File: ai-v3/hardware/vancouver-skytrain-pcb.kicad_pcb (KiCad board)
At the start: 2 copper layers, 150 x 86.2 mm, 85 parts, among them SW1 TS-1187A-B-A-B, SW2 TS-1187A-B-A-B, SW3 TS-1187A-B-A-B, SW4 TS-1187A-B-A-B, U1 XIAO-RP2040-DIP

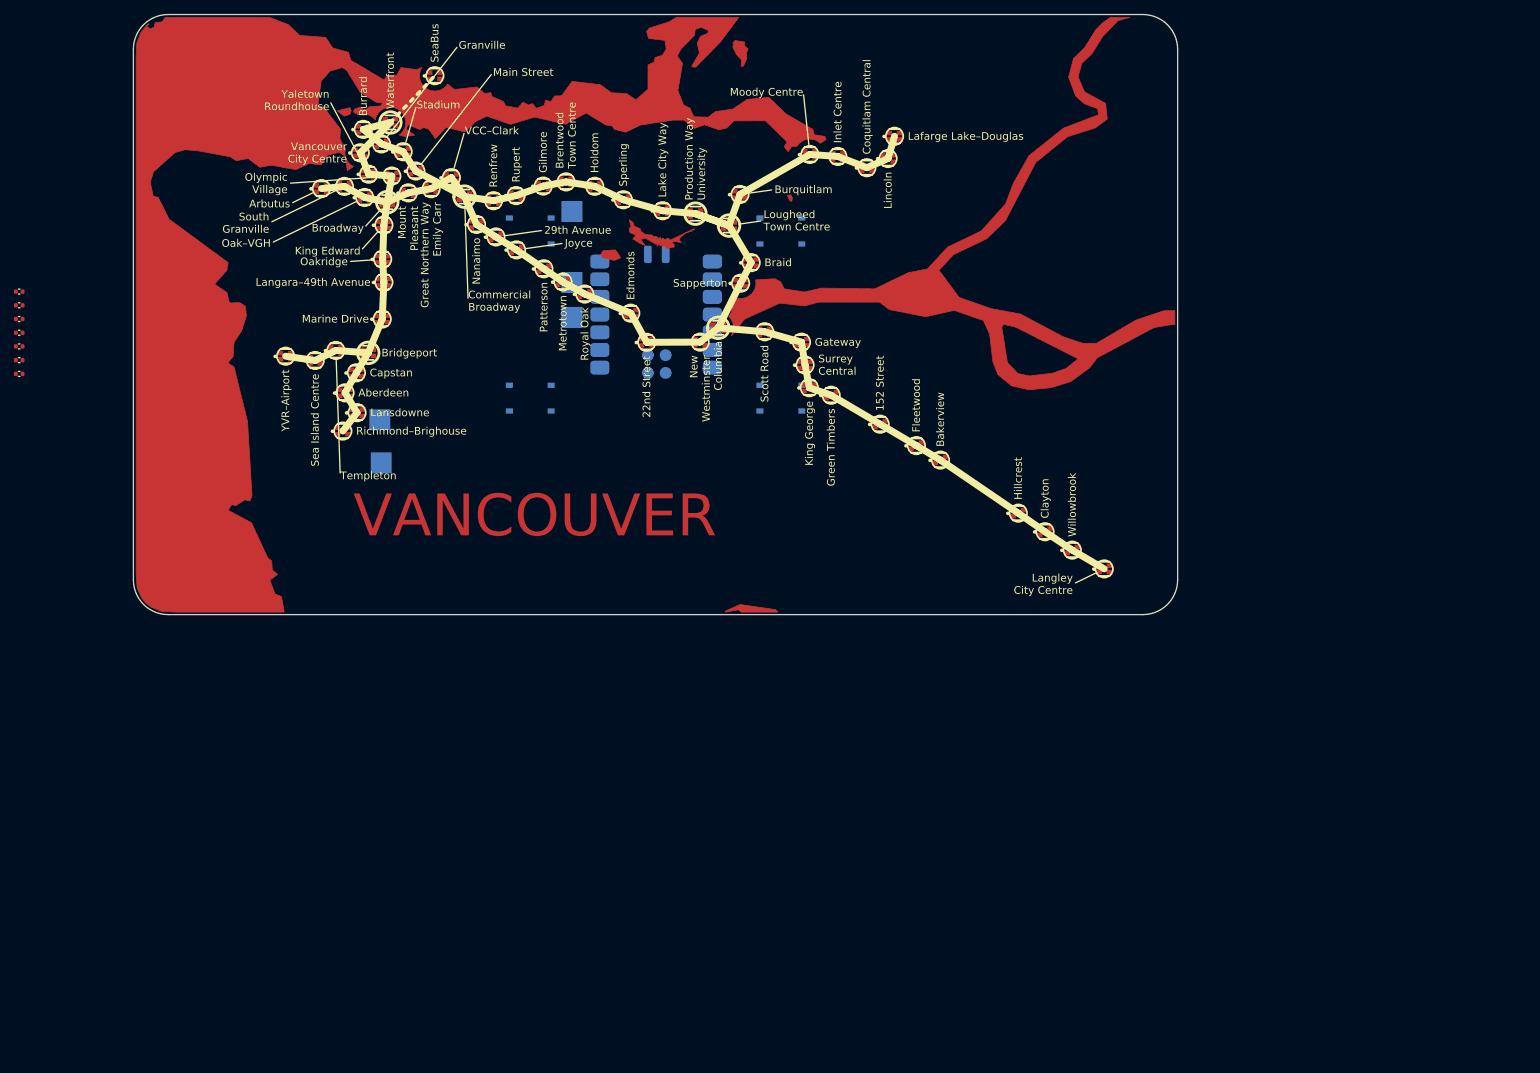
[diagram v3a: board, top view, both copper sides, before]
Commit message: ai-v3: 200 x 109 mm board from the FWA/OSM data build
Board regenerated at board_scale 2.0 from vancouver.json (BC Freshwater
Atlas geography, OSM stations, copper city labels, UBC boundary,
wordmark): placement, outline, art. Wordmark is shifted off the Fraser
South Arm (KiCad's bold stroke font is ~0.95 x size per character, the
estimate was 0.85). DRC: no clearance / edge / shorting violations; art
regeneration idempotent; version 2026-Sep-07. Test margin and README run
commands updated for the new scale. Station labels are left for hand
placement in the PCB.

Co-Authored-By: Claude Fable 5.1 <noreply@anthropic.com>
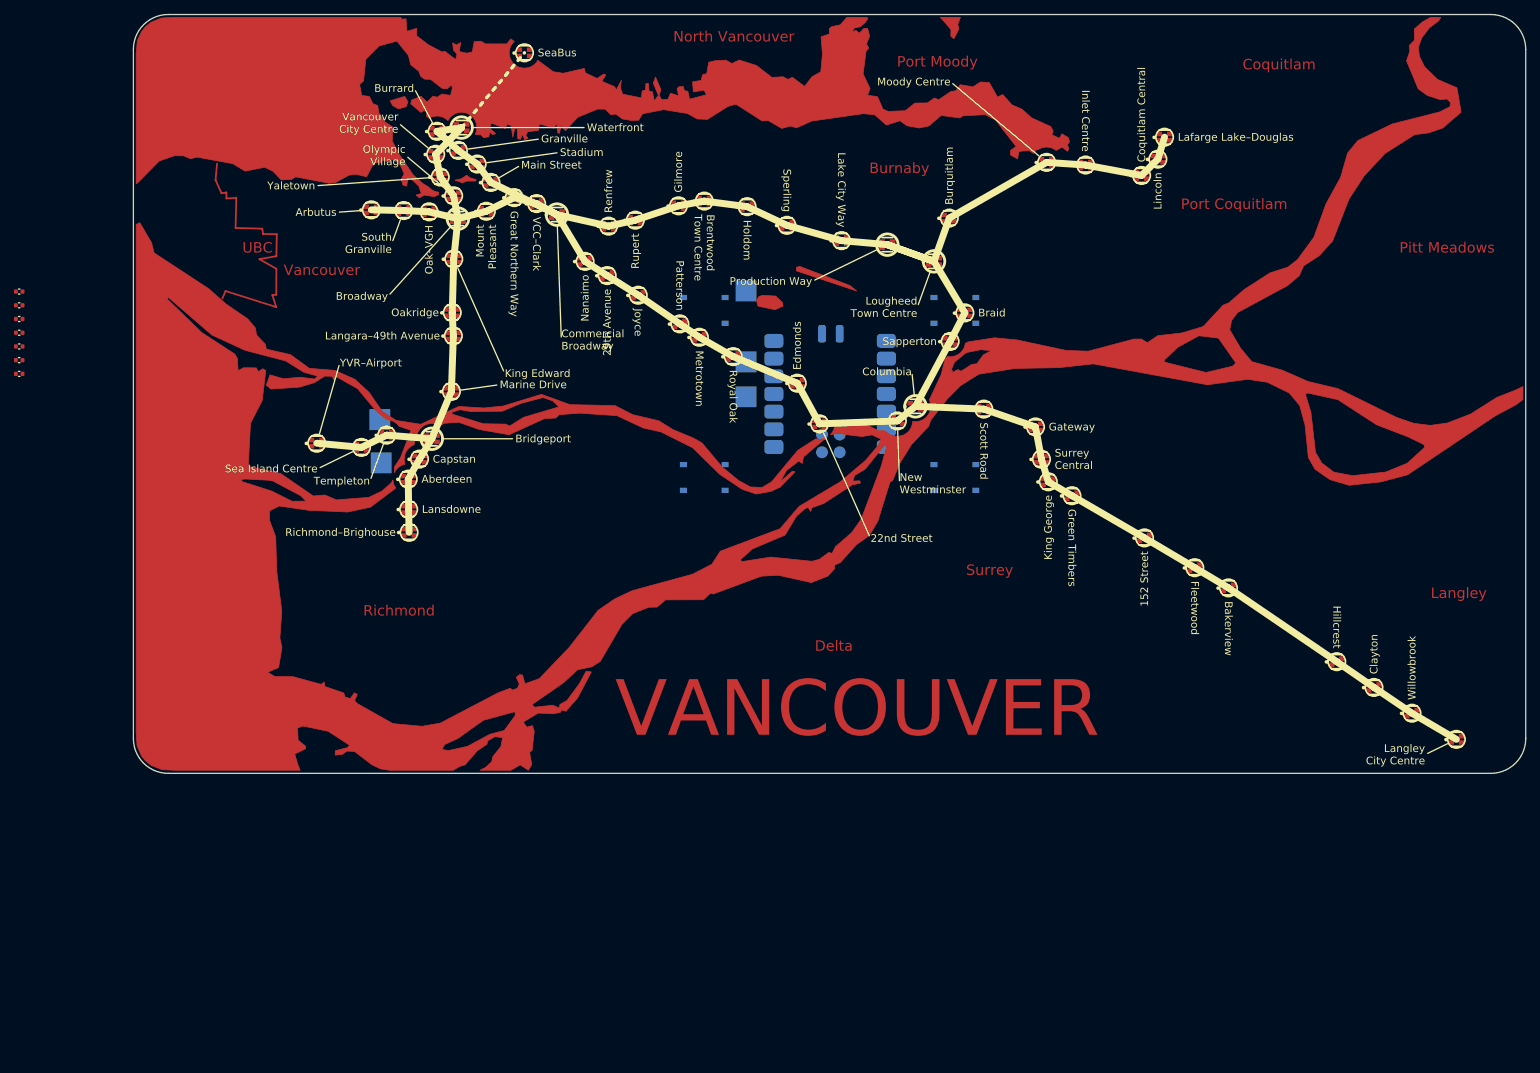
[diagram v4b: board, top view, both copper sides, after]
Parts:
- moved LED29 56.2 mm to (190.0, 104.1)
- moved LED28 54.1 mm to (183.7, 100.4)
- moved LED27 52.3 mm to (178.2, 96.7)
- moved LED26 50.5 mm to (172.9, 93.0)
- moved LED25 45.3 mm to (157.3, 82.4)
- moved LED24 43.7 mm to (152.5, 79.5)
- moved LED23 41.3 mm to (145.2, 75.2)
- moved LED37 39.5 mm to (144.8, 23.1)
- moved LED39 38.8 mm to (148.1, 17.6)
- moved LED38 38.8 mm to (147.2, 20.8)
- moved LED22 37.5 mm to (134.8, 69.1)
- moved LED21 36.9 mm to (131.4, 67.1)
- moved LED20 36.6 mm to (130.4, 63.9)
- moved LED19 35.7 mm to (129.6, 59.2)
- moved LED36 35.6 mm to (136.8, 21.6)
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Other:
- board size 150 x 86.2 mm -> 200 x 109 mm
- board text added: "Burnaby"
- board text added: "Coquitlam"
- board text added: "Delta"
- board text added: "Great Northern Way"
- board text added: "Langley"
- board text added: "North Vancouver"
- board text added: "Pitt Meadows"
- board text added: "Port Coquitlam"
- board text added: "Port Moody"
- board text added: "Production Way"
- board text added: "Richmond"
- board text added: "Surrey"
- board text added: "UBC"
- board text added: "Vancouver"
- board text added: "Vancouver Skytrain Github.com/Funvill/Vancouver-Skytrain-PCB Version: 2026-Sep-07"
- board text added: "Yaletown"
- board text removed: "Great Northern Way Emily Carr"
- board text removed: "Production Way University"
- board text removed: "Vancouver Skytrain Github.com/Funvill/Vancouver-Skytrain-PCB Version: 2026-Sep-06b"
- board text removed: "Yaletown Roundhouse"
